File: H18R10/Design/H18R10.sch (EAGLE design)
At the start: 35 parts, among them P2 HEXABIT_X2_P1_P5, U1 STM32G0B1CEU6NUFQFPN48_STM32_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, U2 L298P, U3 MC7805CD2TR4G, X1 XTALL_CSTCE8M00G52

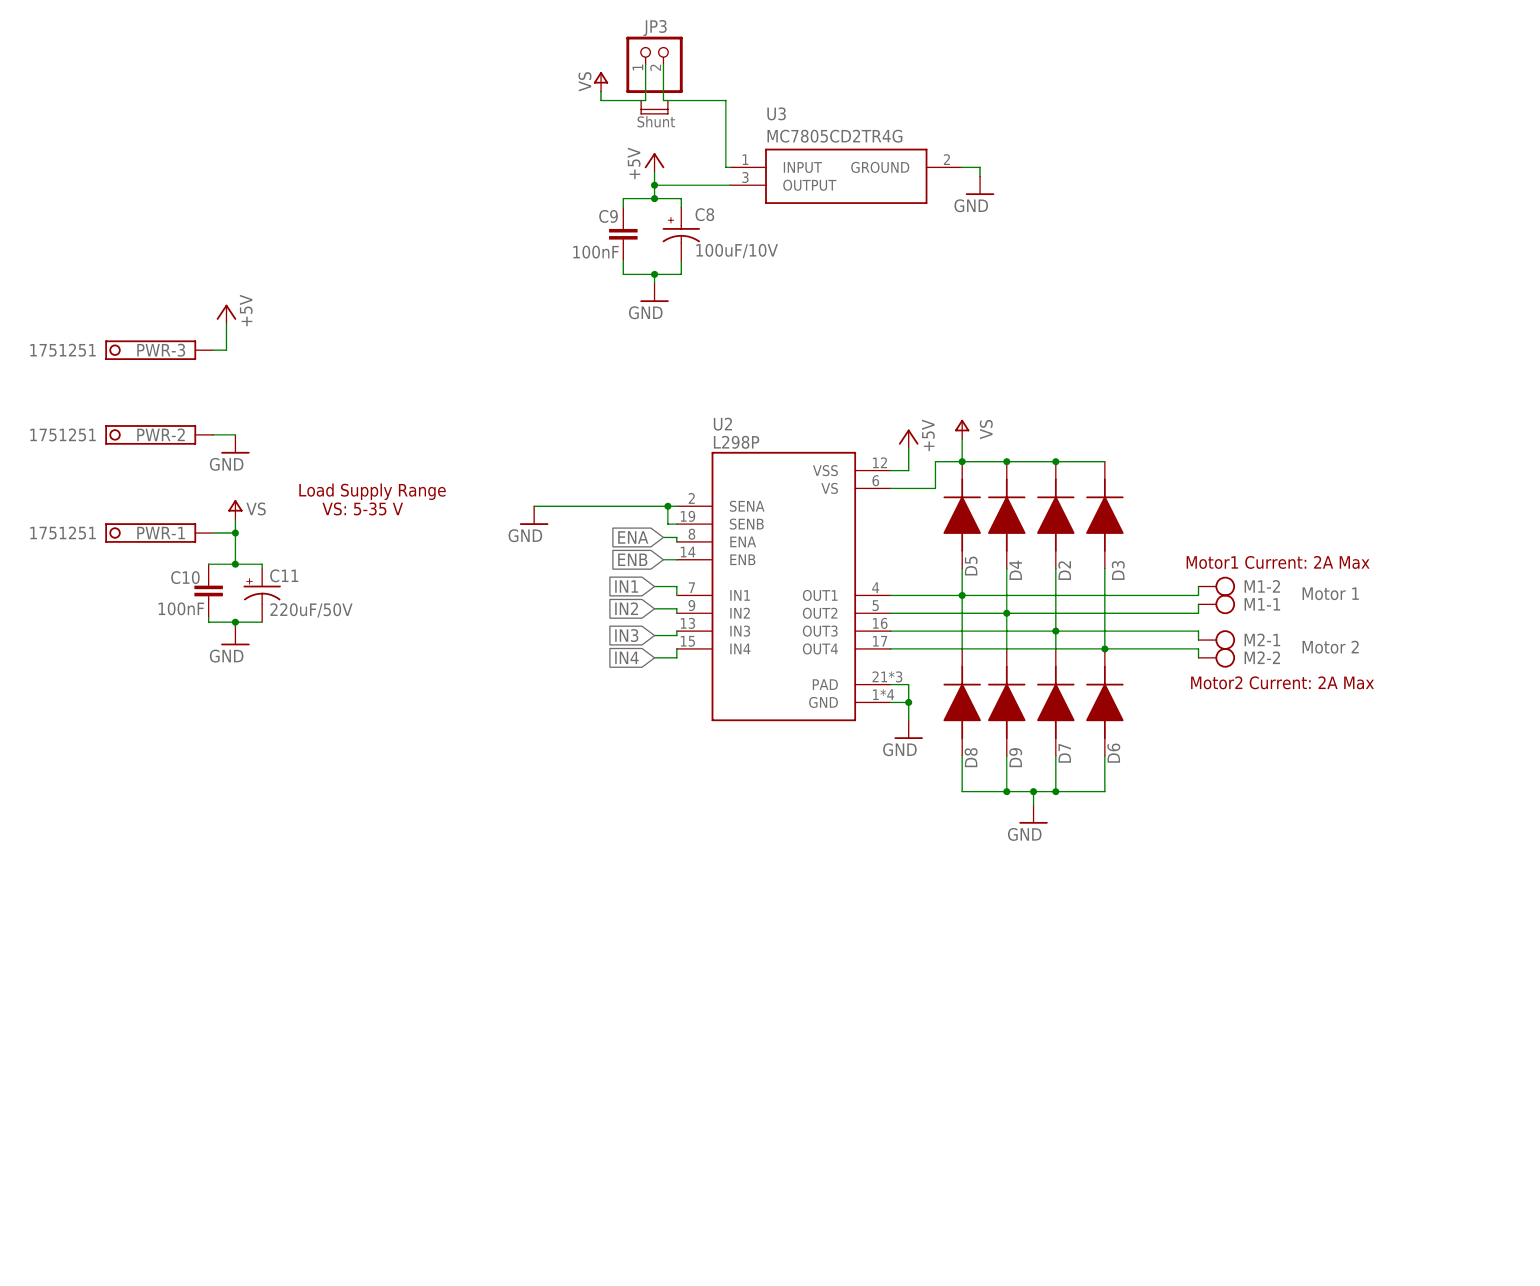
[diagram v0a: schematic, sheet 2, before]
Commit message: -Adding a heatsink - replace the MC7805 with LM2775 IC
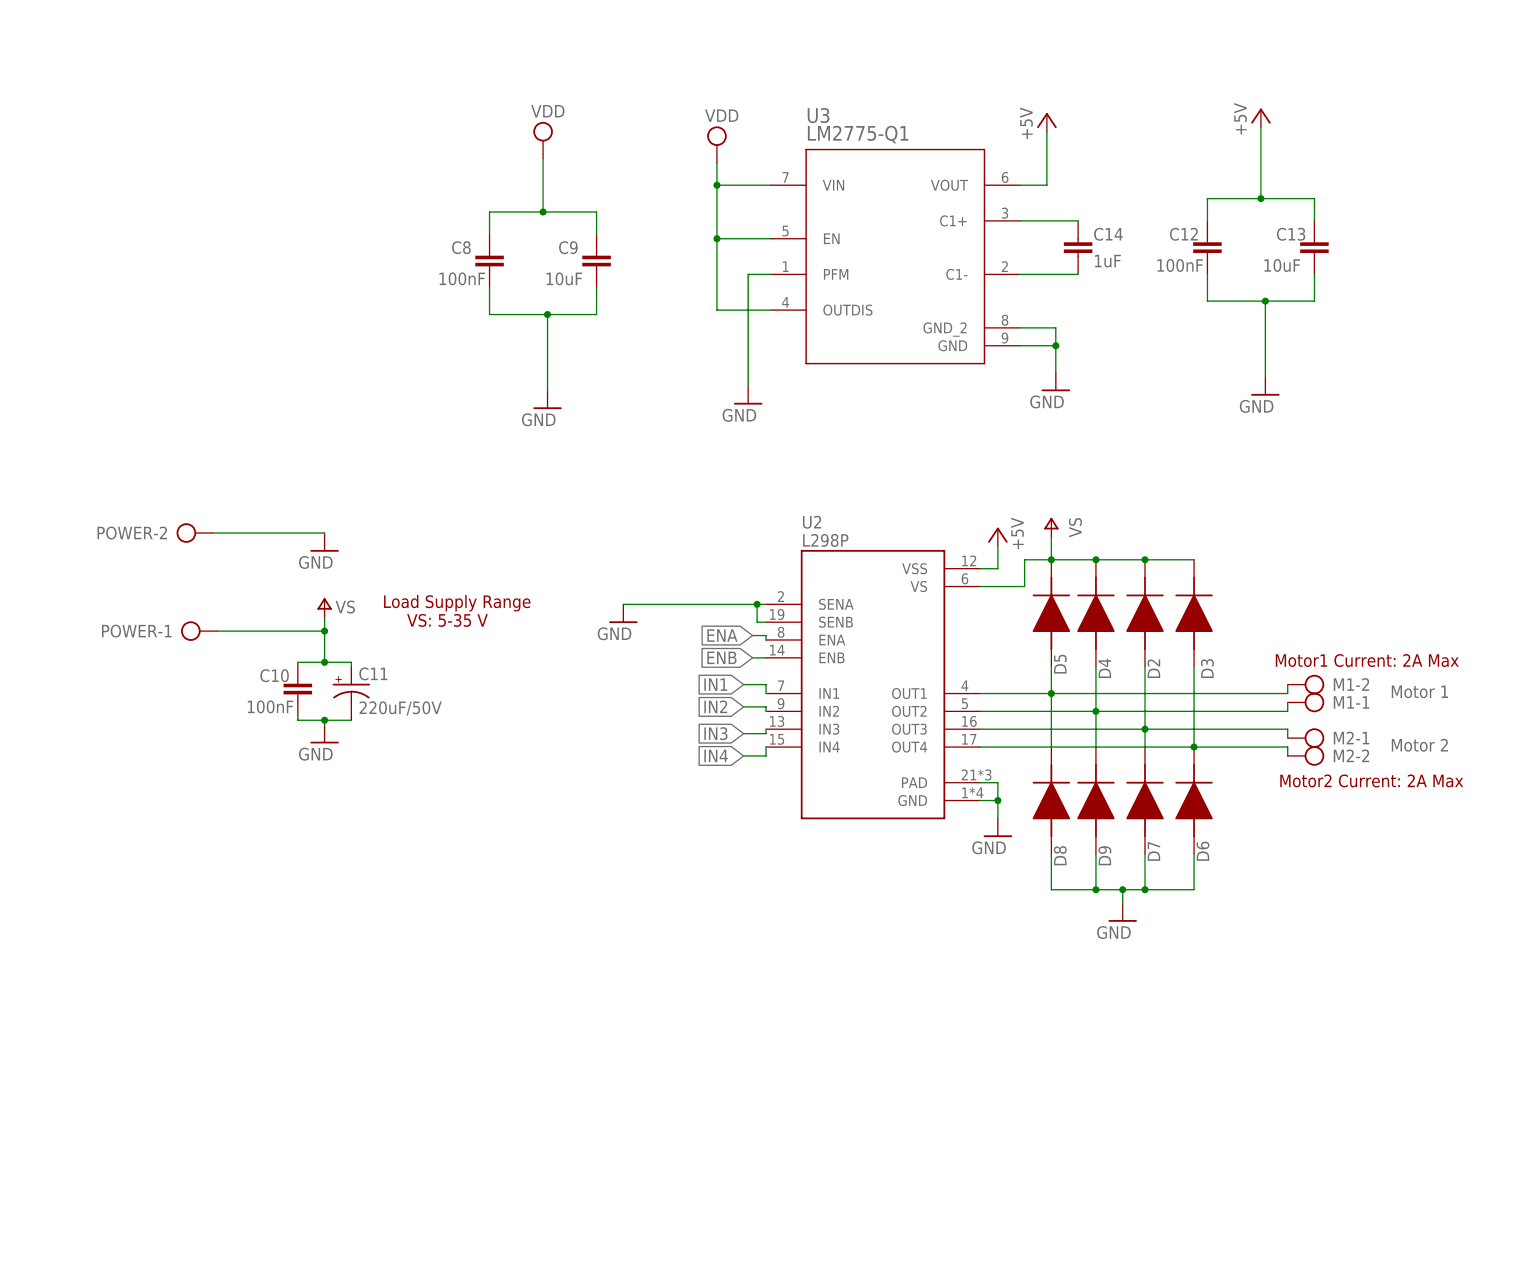
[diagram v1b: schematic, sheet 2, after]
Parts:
- removed JP3: (no value), pinhead:PINHD-1X2(ROUND)
- removed PWR: 1751251, HEXABITZ_CONNECTION_PARTS:1751251
- added C12: 100nF, HEXABITZ_RCLS:C-0603
- added C13: 10uF, HEXABITZ_RCLS:C-0603
- added C14: 1uF, HEXABITZ_RCLS:C-0603
- added POWER: (no value), HEXABITZ_CONNECTION_PARTS:AK500/2
- C8: value 100uF/10V -> 100nF; device HEXABITZ_RCLS:EEUFM1A101 -> HEXABITZ_RCLS:C-0603
- C9: value 100nF -> 10uF
- U3: value MC7805CD2TR4G -> LM2775-Q1; device HEXABITZ_ICs:MC7805CD2TR4G -> HEXABITZ_ICs:LM2775QDSGRQ1
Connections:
- removed net N$12: JP3.2, U3.INPUT
- new net N$3: C14.2, U3.C1-
- new net N$4: C14.1, U3.C1+
- net +5V: now also C12.1, C13.1, U3.VOUT; no longer C8.P, C9.1, PWR-3.K, U3.OUTPUT
- net GND: now also C12.2, C13.2, C8.2, POWER-2.KL, U1.PB12, U1.PB13, U3.GND, U3.GND_2, U3.PFM; no longer C8.N, PWR-2.K, U3.GROUND
- net V+: now also POWER-1.KL; no longer JP3.1, PWR-1.K
- net VDD: now also C8.1, C9.1, U3.EN, U3.OUTDIS, U3.VIN
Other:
- note added: "VDD=3.3 Volt"
- note removed: "Shunt"
- moved on the sheet: C10, C11, C9, D2, D3, D4, D5, D6, D7, D8, D9, M1-1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

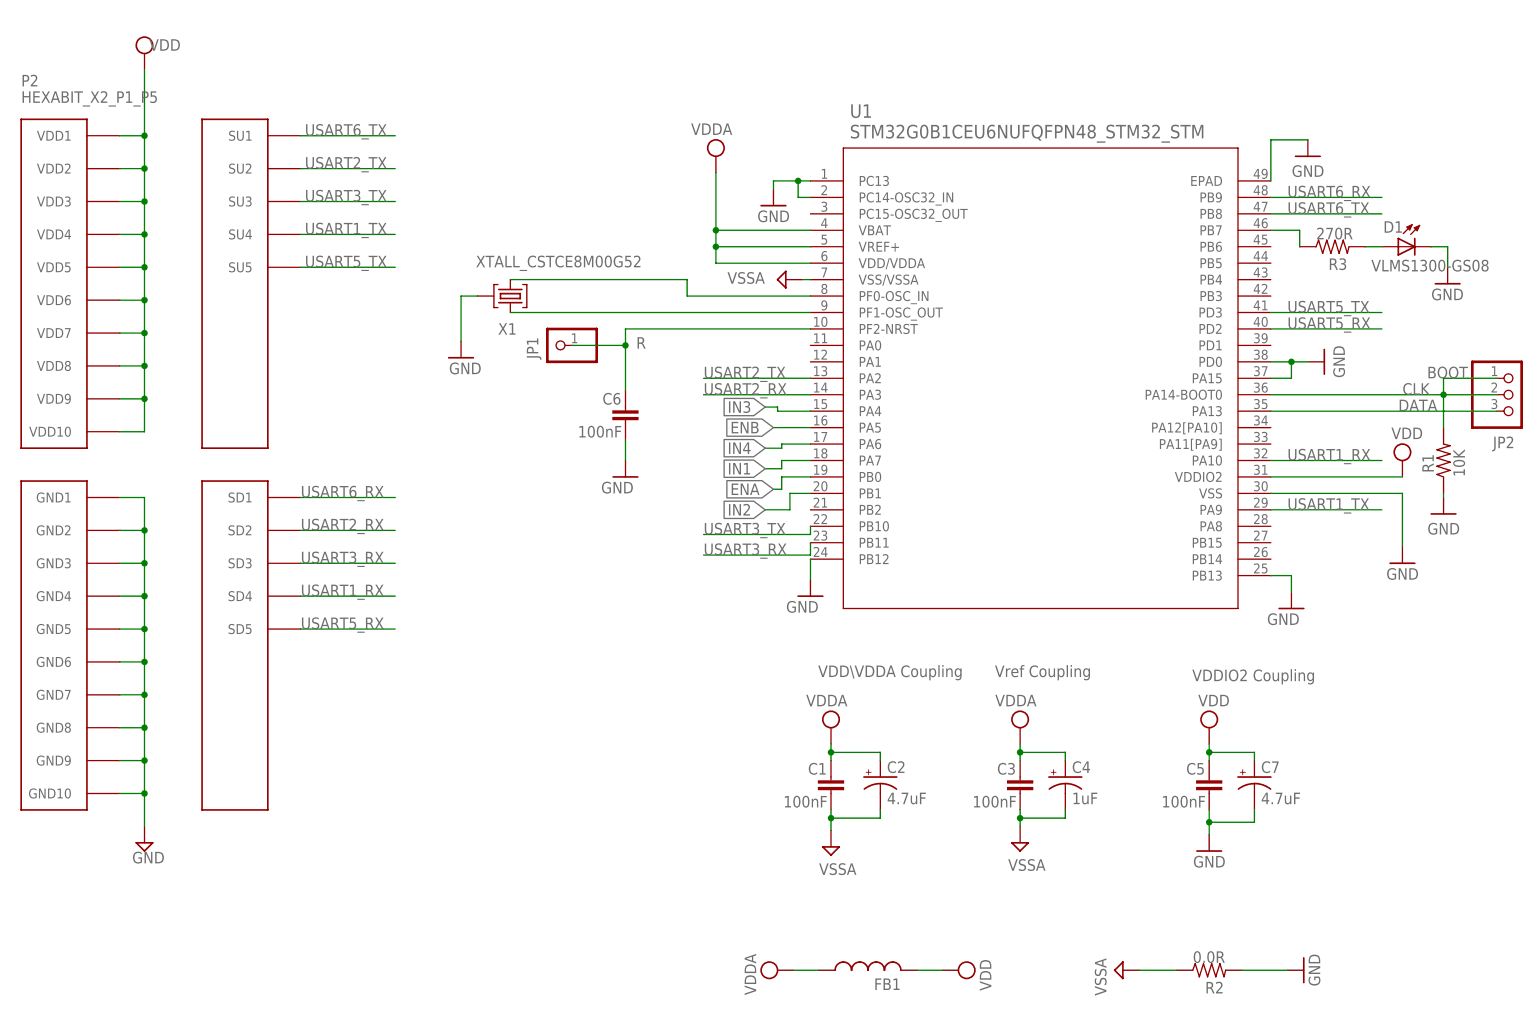
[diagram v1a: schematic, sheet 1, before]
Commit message: -Improving the layout desin and adding TVSs at the MCU GPIOs that connected to the driver IC inputs, and across its supply pins all to increase the imunity against the high spikes.
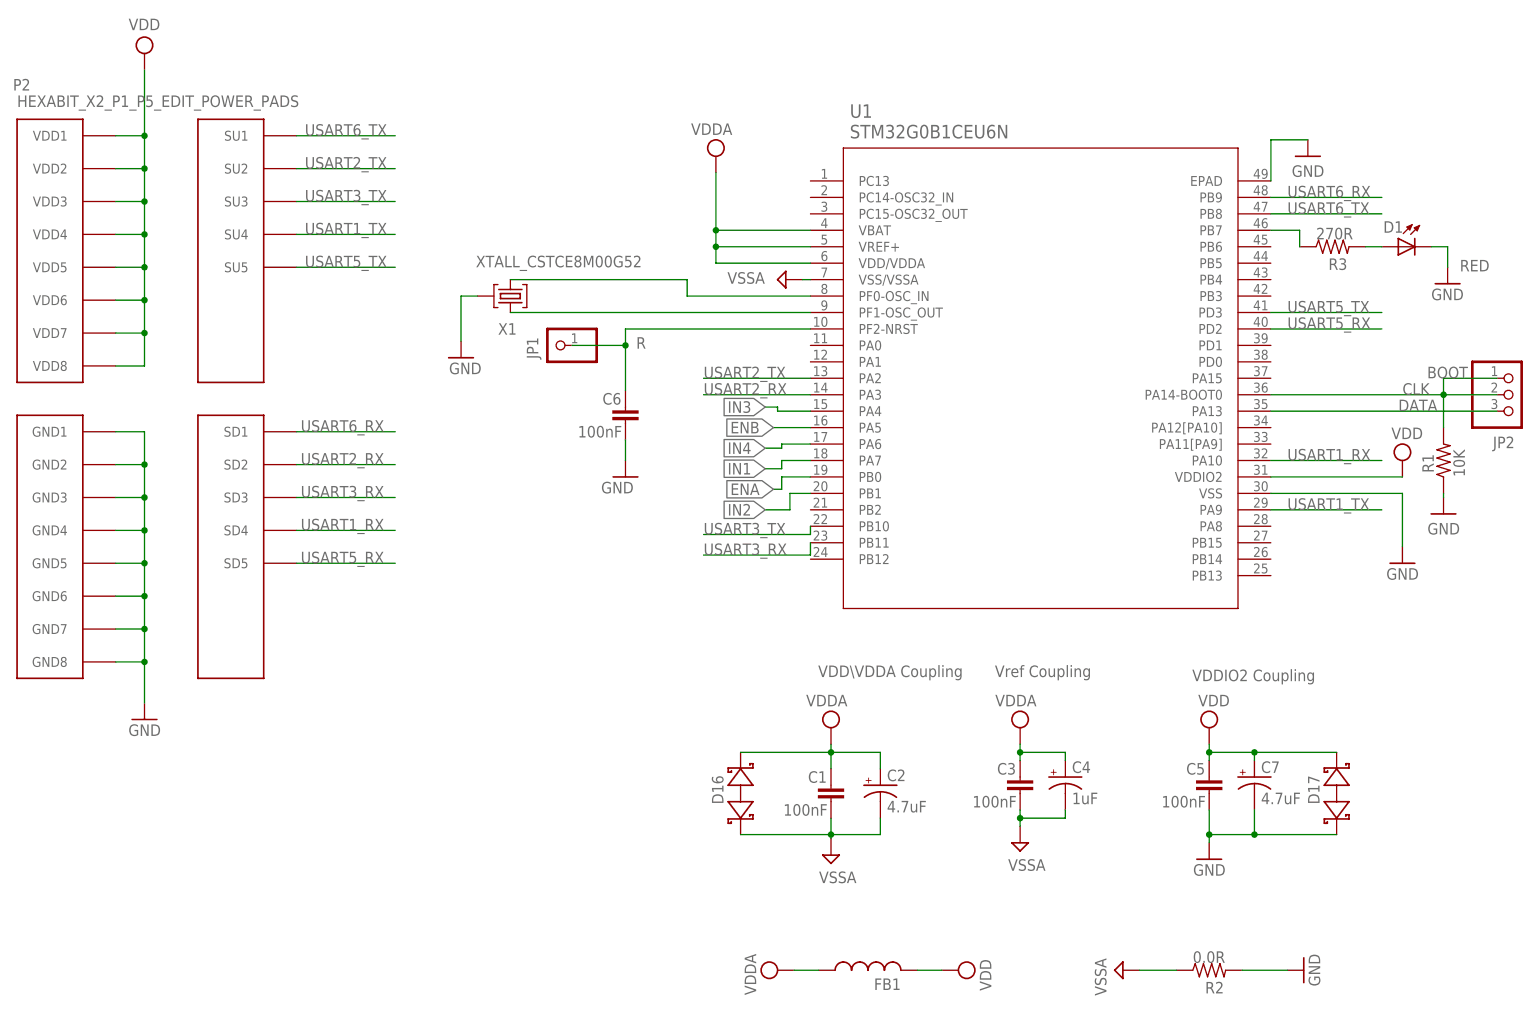
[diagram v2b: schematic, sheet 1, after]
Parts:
- added D10, D11, D12, D13, D14, D15, D16, D17: BOURNS_CDSOD323-T03SCBOURNS_CDSOD323-T03SC_0_0, HEXABITZ_RCLS:BOURNS_CDSOD323-T03SCBOURNS_CDSOD323-T03SC_0_0
- D1: value VLMS1300-GS08 -> RED
- D2, D3, D4, D5, D6, D7, D8, D9: value MBR120ESFT1G -> DIOD-SOD-123; device HEXABITZ_RCLS:MBR120ESFT1G -> HEXABITZ_RCLS:DIOD-SOD-123
- P2: value HEXABIT_X2_P1_P5 -> HEXABIT_X2_P1_P5_EDIT_POWER_PADS; device hexabitz_connectors:HEXABIT_X2_P1_P5 -> hexabitz_connectors:HEXABIT_X2_P1_P5_EDIT_POWER_PADS
- U1: value STM32G0B1CEU6NUFQFPN48_STM32_STM -> STM32G0B1CEU6N; device HEXABITZ_ICs:STM32G0B1CEU6NUFQFPN48_STM32_STM -> HEXABITZ_ICs:STM32G0B1CEU6N
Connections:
- removed net N$16: D3.A, D6.K, M2-2.KL, U2.OUT4
- new net N$7: D5.A, D9.C, M2-2.KL, U2.OUT4
- net ENA: now also D15.C
- net ENB: now also D14.C
- net GND: now also D17.A; no longer C10.2, C11.-, C12.2, C13.2, C8.2, C9.2, D6.A, D7.A, D8.A, D9.A, P2.GND10, P2.GND9, POWER-2.KL, U1.PA15, U1.PB12, U1.PB13, U1.PC13, U1.PC14-OSC32_IN, U1.PD0, U2.GND, U2.PAD, U2.SENA, U2.SENB, U3.GND, U3.GND_2, U3.PFM
- net IN1: now also D13.C
- net IN2: now also D12.C
- net IN3: now also D11.C
- net IN4: now also D10.C
- net N$13: now also D3.A, D7.C; no longer D4.A, D9.K
- net N$14: now also D4.A, D8.C; no longer D2.A, D7.K
- net N$15: now also D2.A, D6.C; no longer D5.A, D8.K
- net V+: now also D2.C, D3.C, D4.C, D5.C; no longer D2.K, D3.K, D4.K, D5.K
- net VDD: now also D17.C; no longer C8.1, C9.1, P2.VDD10, P2.VDD9, U3.EN, U3.OUTDIS, U3.VIN
- net VDDA: now also C8.1, C9.1, D16.C, U3.EN, U3.OUTDIS, U3.VIN
- net VSSA: now also C10.2, C11.-, C12.2, C13.2, C8.2, C9.2, D10.A, D11.A, D12.A, D13.A, D14.A, D15.A, D16.A, D6.A, D7.A, D8.A, D9.A, POWER-2.KL, U2.GND, U2.PAD, U2.SENA, U2.SENB, U3.GND, U3.GND_2, U3.PFM
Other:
- moved on the sheet: C1, C2, D2, D3, D4, D5, D6, D7, D8, D9
